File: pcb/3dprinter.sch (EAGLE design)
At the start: 119 parts, among them IC1 NRF51822, IC1_REG REGULATOR, IC2_REG LP2985-3V3, Q1_BED MOSFET, Q1_FAN1 MOSFETSOT23, Q1_FAN2 MOSFETSOT23, Q1_NOZ MOSFET, Y1 CRYSTAL

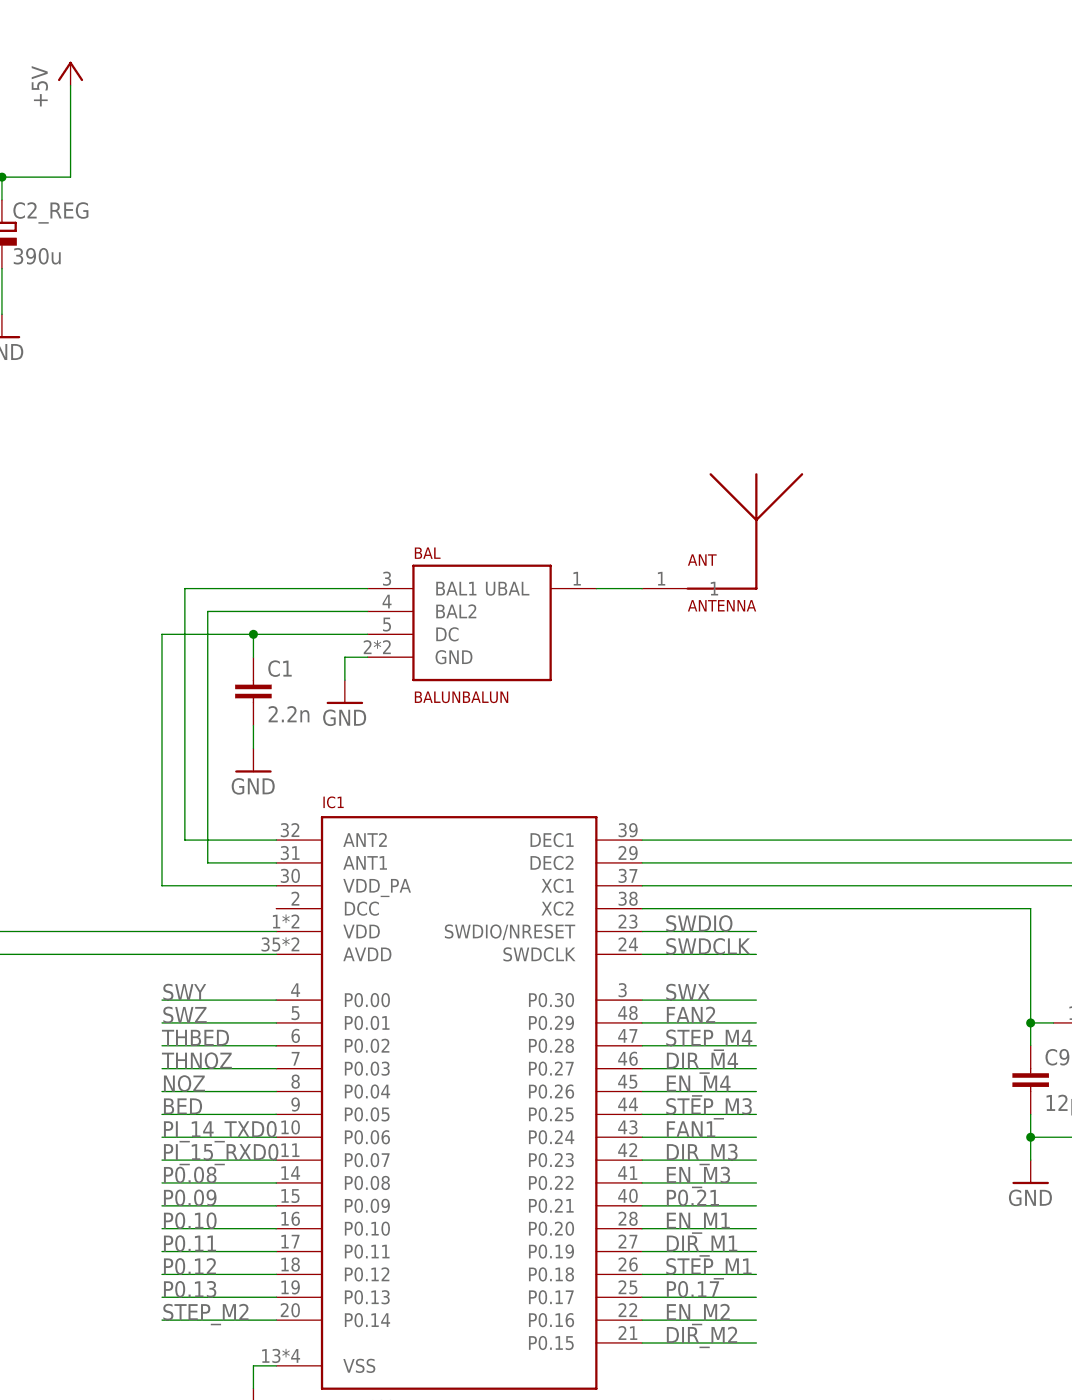
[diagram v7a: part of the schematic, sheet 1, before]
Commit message: Added button and led
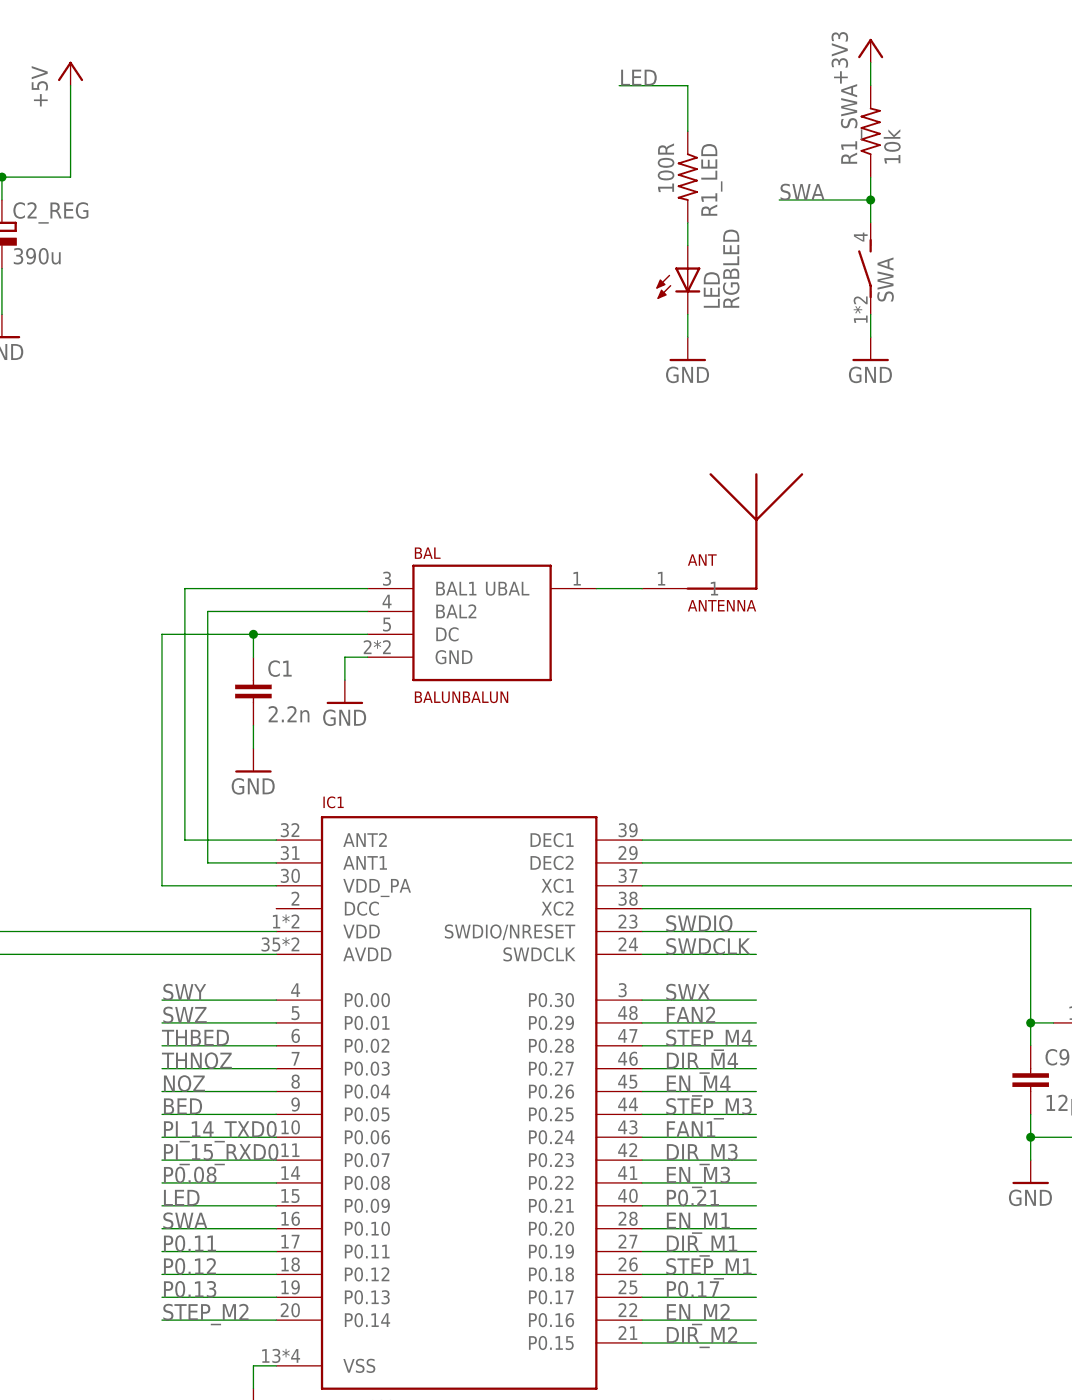
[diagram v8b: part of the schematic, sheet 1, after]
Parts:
- added LED: RGBLED, 3dprinter:RGBLED
- added R1_LED: 100R, 3dprinter:R-US_R0603
- added R1_SWA: 10k, 3dprinter:R-US_R0603
- added SWA: BUTTON, 3dprinter:BUTTON
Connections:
- removed net P0.09: IC1.P0.09
- removed net P0.10: IC1.P0.10
- new net LED: IC1.P0.09, R1_LED.1
- new net LEDA: LED.A, R1_LED.2
- new net SWA: IC1.P0.10, R1_SWA.1, SWA.2
- net +3V3: now also R1_SWA.2
- net GND: now also LED.C, SWA.1
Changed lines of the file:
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@@
 <setting verticaltext="up"/>
 </settings>
-<grid distance="0.1" unitdist="inch" unit="inch" style="lines" multiple="1" display="no" altdistance="0.01" altunitdist="inch" altunit="inch"/>
+<grid distance="0.1" unitdist="inch" unit="inch" style="lines" multiple="1" display="yes" altdistance="0.01" altunitdist="inch" altunit="inch"/>
 <layers>
 <layer number="1" name="Top" color="4" fill="1" visible="no" active="no"/>
@@
 <part name="COPå42" library="supply" deviceset="GND" device=""/>
 <part name="COPå43" library="supply" deviceset="GND" device=""/>
+<part name="SWA" library="3dprinter" deviceset="BUTTON" device=""/>
+<part name="R1_SWA" library="3dprinter" deviceset="R-US_" device="R0603" value="10k"/>
+<part name="GND38" library="supply" deviceset="GND" device=""/>
+<part name="+3V20" library="supply" deviceset="+3V3" device=""/>
+<part name="LED" library="3dprinter" deviceset="RGBLED" device=""/>
+<part name="R1_LED" library="3dprinter" deviceset="R-US_" device="R0603" value="100R"/>
+<part name="GND39" library="supply" deviceset="GND" device=""/>
 </parts>
 <sheets>
@@
 <instance part="+3V6" gate="G$1" x="104.14" y="91.44"/>
 <instance part="+3V7" gate="G$1" x="43.18" y="91.44"/>
+<instance part="SWA" gate="G$1" x="226.06" y="228.6"/>
+<instance part="R1_SWA" gate="G$1" x="226.06" y="243.84" rot="R90"/>
+<instance part="GND38" gate="1" x="226.06" y="218.44"/>
+<instance part="+3V20" gate="G$1" x="226.06" y="254"/>
+<instance part="LED" gate="G$1" x="205.74" y="228.6"/>
+<instance part="R1_LED" gate="G$1" x="205.74" y="238.76" rot="R270"/>
+<instance part="GND39" gate="1" x="205.74" y="218.44"/>
 </instances>
 <busses>
@@
 <wire x1="104.14" y1="71.12" x2="104.14" y2="68.58" width="0.1524" layer="91"/>
 </segment>
+<segment>
+<pinref part="GND38" gate="1" pin="GND"/>
+<pinref part="SWA" gate="G$1" pin="1"/>
+<wire x1="226.06" y1="220.98" x2="226.06" y2="223.52" width="0.1524" layer="91"/>
+</segment>
+<segment>
+<pinref part="GND39" gate="1" pin="GND"/>
+<pinref part="LED" gate="G$1" pin="C"/>
+<wire x1="205.74" y1="223.52" x2="205.74" y2="220.98" width="0.1524" layer="91"/>
+</segment>
 </net>
 <net name="+3V3" class="0">
@@
 <pinref part="+3V6" gate="G$1" pin="+3V3"/>
 <wire x1="104.14" y1="86.36" x2="104.14" y2="88.9" width="0.1524" layer="91"/>
+</segment>
+<segment>
+<pinref part="R1_SWA" gate="G$1" pin="2"/>
+<wire x1="226.06" y1="248.92" x2="226.06" y2="251.46" width="0.1524" layer="91"/>
+<pinref part="+3V20" gate="G$1" pin="+3V3"/>
 </segment>
 </net>
@@
 </segment>
 </net>
-<net name="P0.09" class="0">
+<net name="STEP_M4" class="0">
+<segment>
+<pinref part="IC1" gate="G$1" pin="P0.28"/>
+<wire x1="213.36" y1="142.24" x2="200.66" y2="142.24" width="0.1524" layer="91"/>
+<label x="203.2" y="142.24" size="1.778" layer="95"/>
+</segment>
+</net>
+<net name="DIR_M4" class="0">
+<segment>
+<pinref part="IC1" gate="G$1" pin="P0.27"/>
+<wire x1="213.36" y1="139.7" x2="200.66" y2="139.7" width="0.1524" layer="91"/>
+<label x="203.2" y="139.7" size="1.778" layer="95"/>
+</segment>
+</net>
+<net name="P0.21" class="0">
+<segment>
+<pinref part="IC1" gate="G$1" pin="P0.21"/>
+<wire x1="213.36" y1="124.46" x2="200.66" y2="124.46" width="0.1524" layer="91"/>
+<label x="203.2" y="124.46" size="1.778" layer="95"/>
+</segment>
+</net>
+<net name="EN_M4" class="0">
+<segment>
+<pinref part="IC1" gate="G$1" pin="P0.26"/>
+<wire x1="213.36" y1="137.16" x2="200.66" y2="137.16" width="0.1524" layer="91"/>
+<label x="203.2" y="137.16" size="1.778" layer="95"/>
+</segment>
+</net>
+<net name="DIR_M3" class="0">
+<segment>
+<pinref part="IC1" gate="G$1" pin="P0.23"/>
+<wire x1="213.36" y1="129.54" x2="200.66" y2="129.54" width="0.1524" layer="91"/>
+<label x="203.2" y="129.54" size="1.778" layer="95"/>
+</segment>
+</net>
+<net name="P0.08" class="0">
+<segment>
+<pinref part="IC1" gate="G$1" pin="P0.08"/>
+<wire x1="160.02" y1="127" x2="147.32" y2="127" width="0.1524" layer="91"/>
+<label x="147.32" y="127" size="1.778" layer="95"/>
+</segment>
+</net>
+<net name="P0.17" class="0">
+<segment>
+<pinref part="IC1" gate="G$1" pin="P0.17"/>
+<wire x1="213.36" y1="114.3" x2="200.66" y2="114.3" width="0.1524" layer="91"/>
+<label x="203.2" y="114.3" size="1.778" layer="95"/>
+</segment>
+</net>
+<net name="P0.13" class="0">
+<segment>
+<pinref part="IC1" gate="G$1" pin="P0.13"/>
+<wire x1="160.02" y1="114.3" x2="147.32" y2="114.3" width="0.1524" layer="91"/>
+<label x="147.32" y="114.3" size="1.778" layer="95"/>
+</segment>
+</net>
+<net name="SWA" class="0">
+<segment>
+<pinref part="R1_SWA" gate="G$1" pin="1"/>
+<wire x1="226.06" y1="236.22" x2="226.06" y2="238.76" width="0.1524" layer="91"/>
+<wire x1="226.06" y1="236.22" x2="215.9" y2="236.22" width="0.1524" layer="91"/>
+<label x="215.9" y="236.22" size="1.778" layer="95"/>
+<pinref part="SWA" gate="G$1" pin="2"/>
+<wire x1="226.06" y1="236.22" x2="226.06" y2="233.68" width="0.1524" layer="91"/>
+<junction x="226.06" y="236.22"/>
+</segment>
+<segment>
+<pinref part="IC1" gate="G$1" pin="P0.10"/>
+<wire x1="160.02" y1="121.92" x2="147.32" y2="121.92" width="0.1524" layer="91"/>
+<label x="147.32" y="121.92" size="1.778" layer="95"/>
+</segment>
+</net>
+<net name="LEDA" class="0">
+<segment>
+<pinref part="R1_LED" gate="G$1" pin="2"/>
+<pinref part="LED" gate="G$1" pin="A"/>
+<wire x1="205.74" y1="233.68" x2="205.74" y2="231.14" width="0.1524" layer="91"/>
+</segment>
+</net>
+<net name="LED" class="0">
+<segment>
+<pinref part="R1_LED" gate="G$1" pin="1"/>
+<wire x1="205.74" y1="243.84" x2="205.74" y2="248.92" width="0.1524" layer="91"/>
+<label x="198.12" y="248.92" size="1.778" layer="95"/>
+<wire x1="205.74" y1="248.92" x2="198.12" y2="248.92" width="0.1524" layer="91"/>
+</segment>
 <segment>
 <pinref part="IC1" gate="G$1" pin="P0.09"/>
@@
 </segment>
 </net>
-<net name="STEP_M4" class="0">
-<segment>
-<pinref part="IC1" gate="G$1" pin="P0.28"/>
-<wire x1="213.36" y1="142.24" x2="200.66" y2="142.24" width="0.1524" layer="91"/>
-<label x="203.2" y="142.24" size="1.778" layer="95"/>
-</segment>
-</net>
-<net name="DIR_M4" class="0">
-<segment>
-<pinref part="IC1" gate="G$1" pin="P0.27"/>
-<wire x1="213.36" y1="139.7" x2="200.66" y2="139.7" width="0.1524" layer="91"/>
-<label x="203.2" y="139.7" size="1.778" layer="95"/>
-</segment>
-</net>
-<net name="P0.21" class="0">
-<segment>
-<pinref part="IC1" gate="G$1" pin="P0.21"/>
-<wire x1="213.36" y1="124.46" x2="200.66" y2="124.46" width="0.1524" layer="91"/>
-<label x="203.2" y="124.46" size="1.778" layer="95"/>
-</segment>
-</net>
-<net name="EN_M4" class="0">
-<segment>
-<pinref part="IC1" gate="G$1" pin="P0.26"/>
-<wire x1="213.36" y1="137.16" x2="200.66" y2="137.16" width="0.1524" layer="91"/>
-<label x="203.2" y="137.16" size="1.778" layer="95"/>
-</segment>
-</net>
-<net name="DIR_M3" class="0">
-<segment>
-<pinref part="IC1" gate="G$1" pin="P0.23"/>
-<wire x1="213.36" y1="129.54" x2="200.66" y2="129.54" width="0.1524" layer="91"/>
-<label x="203.2" y="129.54" size="1.778" layer="95"/>
-</segment>
-</net>
-<net name="P0.08" class="0">
-<segment>
-<pinref part="IC1" gate="G$1" pin="P0.08"/>
-<wire x1="160.02" y1="127" x2="147.32" y2="127" width="0.1524" layer="91"/>
-<label x="147.32" y="127" size="1.778" layer="95"/>
-</segment>
-</net>
-<net name="P0.10" class="0">
-<segment>
-<pinref part="IC1" gate="G$1" pin="P0.10"/>
-<wire x1="160.02" y1="121.92" x2="147.32" y2="121.92" width="0.1524" layer="91"/>
-<label x="147.32" y="121.92" size="1.778" layer="95"/>
-</segment>
-</net>
-<net name="P0.17" class="0">
-<segment>
-<pinref part="IC1" gate="G$1" pin="P0.17"/>
-<wire x1="213.36" y1="114.3" x2="200.66" y2="114.3" width="0.1524" layer="91"/>
-<label x="203.2" y="114.3" size="1.778" layer="95"/>
-</segment>
-</net>
-<net name="P0.13" class="0">
-<segment>
-<pinref part="IC1" gate="G$1" pin="P0.13"/>
-<wire x1="160.02" y1="114.3" x2="147.32" y2="114.3" width="0.1524" layer="91"/>
-<label x="147.32" y="114.3" size="1.778" layer="95"/>
-</segment>
-</net>
